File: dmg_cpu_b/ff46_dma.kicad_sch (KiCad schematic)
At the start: 71 parts

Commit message: First lot of fixes based on issues found.
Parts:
- removed LYXE: OR_2, symbol DMG_CPU_Cells:OR_2
- added LYXE: NOR_LATCH, symbol DMG_CPU_Cells:NOR_LATCH
- added PYSU: INVERTER_A, symbol DMG_CPU_Cells:INVERTER_A
- gave numbers to parts that had none: 1
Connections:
- net CPU_WR2: now also LAVY.1; no longer LAVY.2
- net FF46: now also LAVY.2; no longer LAVY.1
- net ~{DMA_PHI}: now also NAXY.2
- net at LENE.3 (D), LUVY.6 (Q): no longer NAXY.2
- net at LAPA.1, LOKO.3: now also LYXE.4 (RESET)
- net at MARU.1 (~{ENA}), MARU.3 (ENA), NAFA.1 (~{ENA})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: now also PYSU.2; no longer LORU.2
- net at LAVY.3, LORU.1, LUPA.1: now also LYXE.1 (SET)
- net at LUPA.2: now also LYXE.3 (Q)
- new net: LORU.2, PYSU.1
- no-connect marks 5 -> 6
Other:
- moved on the sheet: LAVY, LORU, LUPA, LUVY, MOLU, NYGO

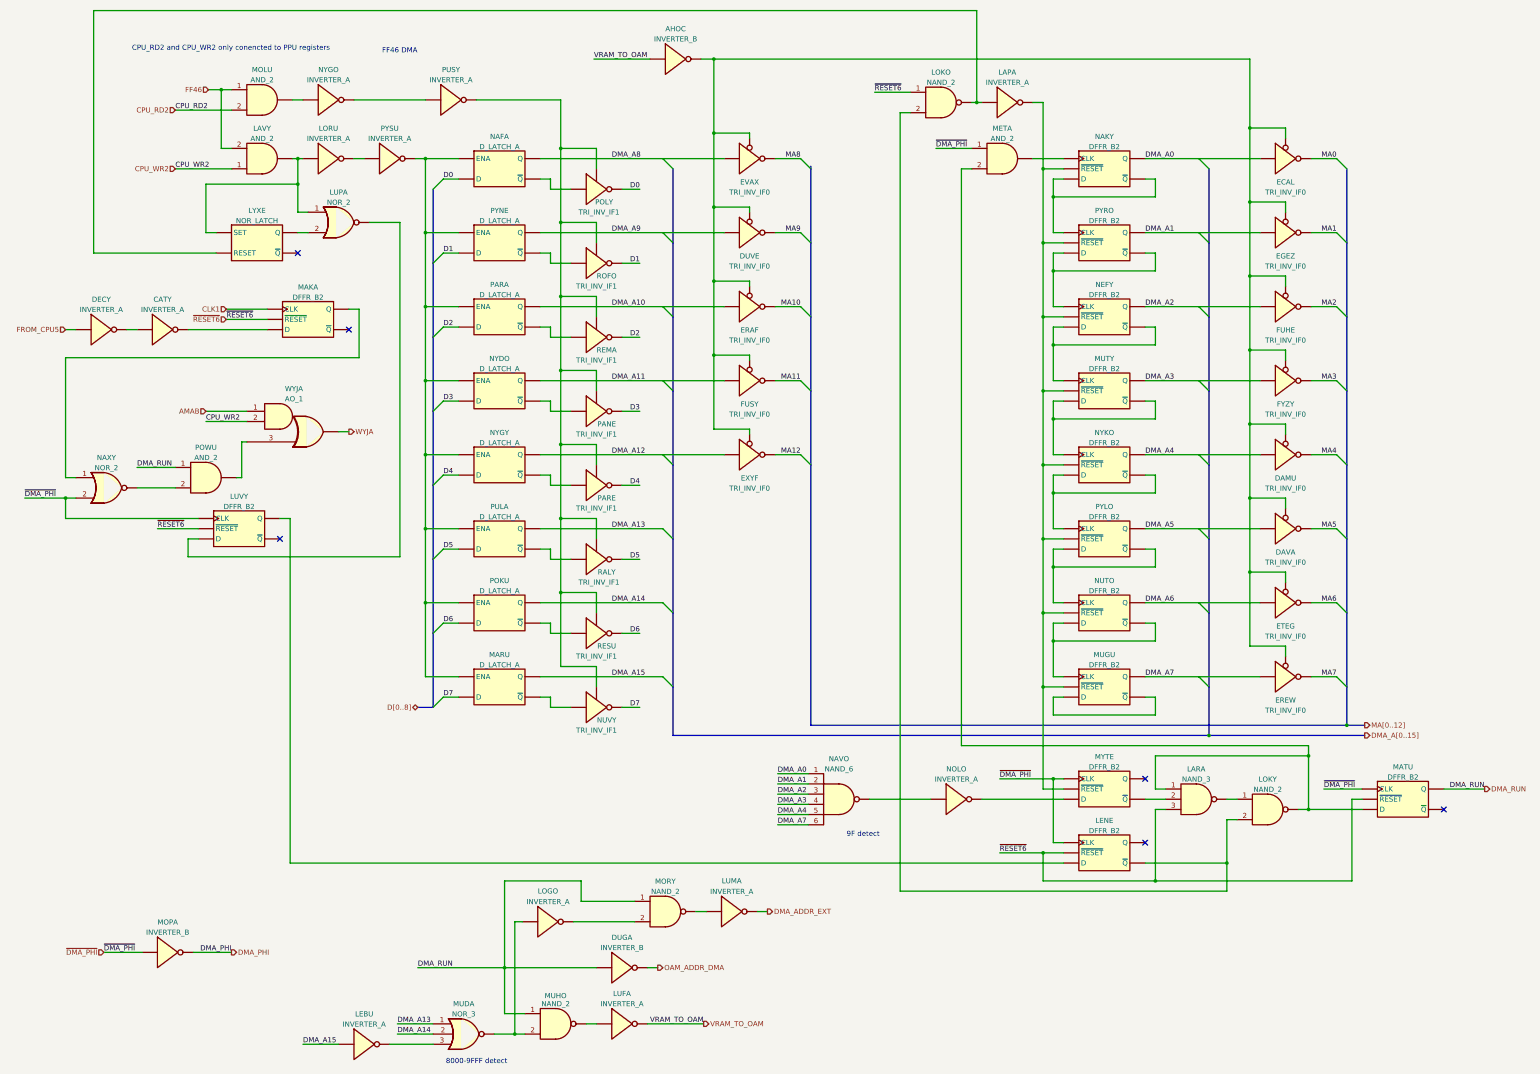
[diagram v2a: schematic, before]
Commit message: CH1 SWEEP page added.
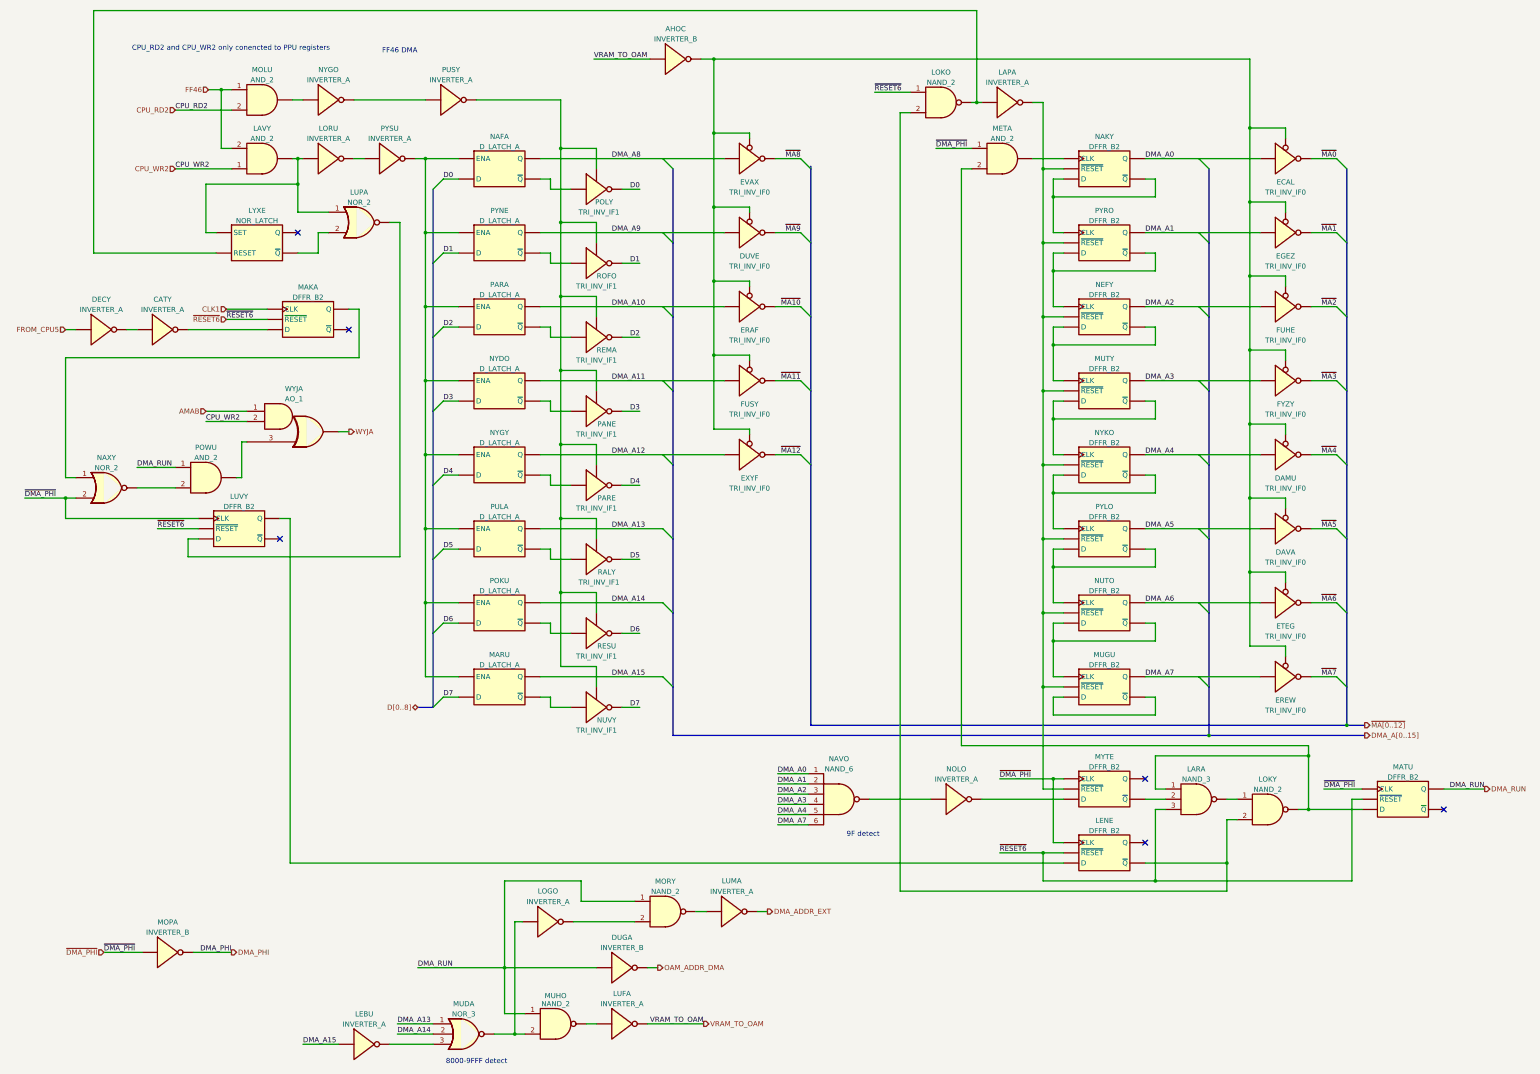
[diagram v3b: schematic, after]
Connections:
- net at LUPA.2: now also LYXE.2 (~{Q}); no longer LYXE.3 (Q)
- net MA0 renamed ~{MA0}
- net MA1 renamed ~{MA1}
- net MA10 renamed ~{MA10}
- net MA11 renamed ~{MA11}
- net MA12 renamed ~{MA12}
- net MA2 renamed ~{MA2}
- net MA3 renamed ~{MA3}
- net MA4 renamed ~{MA4}
- net MA5 renamed ~{MA5}
- net MA6 renamed ~{MA6}
- net MA7 renamed ~{MA7}
- net MA8 renamed ~{MA8}
- net MA9 renamed ~{MA9}
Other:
- moved on the sheet: LUPA
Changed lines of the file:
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@@
   )
   (no_connect (at 106.045 98.425))
-  (no_connect (at 93.345 79.375))
+  (no_connect (at 93.345 74.295))
   (no_connect (at 88.9 150.495))
   (no_connect (at 378.46 217.805))
@@
     (stroke (width 0) (type default) (color 0 0 0 0))
   )
-  (wire (pts (xy 118.745 71.755) (xy 111.125 71.755))
+  (wire (pts (xy 118.745 71.755) (xy 116.205 71.755))
     (stroke (width 0) (type default) (color 0 0 0 0))
   )
@@
     (stroke (width 0) (type default) (color 0 0 0 0))
   )
-  (wire (pts (xy 93.345 74.295) (xy 95.885 74.295))
-    (stroke (width 0) (type default) (color 0 0 0 0))
-  )
   (wire (pts (xy 42.545 19.05) (xy 42.545 79.375))
     (stroke (width 0) (type default) (color 0 0 0 0))
@@
     (stroke (width 0) (type default) (color 0 0 0 0))
   )
+  (wire (pts (xy 98.425 74.295) (xy 100.965 74.295))
+    (stroke (width 0) (type default) (color 0 0 0 0))
+  )
   (wire (pts (xy 144.78 257.175) (xy 144.78 235.585))
     (stroke (width 0) (type default) (color 0 0 0 0))
@@
     (stroke (width 0) (type default) (color 0 0 0 0))
   )
+  (wire (pts (xy 93.345 79.375) (xy 98.425 79.375))
+    (stroke (width 0) (type default) (color 0 0 0 0))
+  )
   (wire (pts (xy 283.845 113.665) (xy 278.765 113.665))
     (stroke (width 0) (type default) (color 0 0 0 0))
@@
     (stroke (width 0) (type default) (color 0 0 0 0))
   )
+  (wire (pts (xy 98.425 79.375) (xy 98.425 74.295))
+    (stroke (width 0) (type default) (color 0 0 0 0))
+  )
   (wire (pts (xy 156.21 171.45) (xy 156.21 173.99))
     (stroke (width 0) (type default) (color 0 0 0 0))
@@
     (stroke (width 0) (type default) (color 0 0 0 0))
   )
-  (wire (pts (xy 95.885 69.215) (xy 93.345 69.215))
+  (wire (pts (xy 100.965 69.215) (xy 93.345 69.215))
     (stroke (width 0) (type default) (color 0 0 0 0))
   )
@@
     (effects (font (size 1.27 1.27)) (justify left bottom))
   )
-  (label "MA5" (at 351.79 147.955 180)
-    (effects (font (size 1.27 1.27)) (justify right bottom))
-  )
-  (label "MA7" (at 351.79 184.785 180)
-    (effects (font (size 1.27 1.27)) (justify right bottom))
-  )
-  (label "MA6" (at 351.79 166.37 180)
+  (label "~{MA5}" (at 351.79 147.955 180)
+    (effects (font (size 1.27 1.27)) (justify right bottom))
+  )
+  (label "~{MA7}" (at 351.79 184.785 180)
+    (effects (font (size 1.27 1.27)) (justify right bottom))
+  )
+  (label "~{MA6}" (at 351.79 166.37 180)
     (effects (font (size 1.27 1.27)) (justify right bottom))
   )
@@
     (effects (font (size 1.27 1.27)) (justify left bottom))
   )
-  (label "MA8" (at 218.44 55.88 180)
+  (label "~{MA8}" (at 218.44 55.88 180)
     (effects (font (size 1.27 1.27)) (justify right bottom))
   )
@@
     (effects (font (size 1.27 1.27)) (justify left bottom))
   )
-  (label "MA2" (at 351.79 92.71 180)
-    (effects (font (size 1.27 1.27)) (justify right bottom))
-  )
-  (label "MA4" (at 351.79 129.54 180)
+  (label "~{MA2}" (at 351.79 92.71 180)
+    (effects (font (size 1.27 1.27)) (justify right bottom))
+  )
+  (label "~{MA4}" (at 351.79 129.54 180)
     (effects (font (size 1.27 1.27)) (justify right bottom))
   )
@@
     (effects (font (size 1.27 1.27)) (justify left bottom))
   )
-  (label "MA10" (at 218.44 92.71 180)
+  (label "~{MA10}" (at 218.44 92.71 180)
     (effects (font (size 1.27 1.27)) (justify right bottom))
   )
@@
     (effects (font (size 1.27 1.27)) (justify left bottom))
   )
-  (label "MA12" (at 218.44 129.54 180)
+  (label "~{MA12}" (at 218.44 129.54 180)
     (effects (font (size 1.27 1.27)) (justify right bottom))
   )
@@
     (effects (font (size 1.27 1.27)) (justify left bottom))
   )
-  (label "MA11" (at 218.44 111.125 180)
+  (label "~{MA11}" (at 218.44 111.125 180)
     (effects (font (size 1.27 1.27)) (justify right bottom))
   )
@@
     (effects (font (size 1.27 1.27)) (justify right bottom))
   )
-  (label "MA9" (at 218.44 74.295 180)
-    (effects (font (size 1.27 1.27)) (justify right bottom))
-  )
-  (label "MA0" (at 351.79 55.88 180)
+  (label "~{MA9}" (at 218.44 74.295 180)
+    (effects (font (size 1.27 1.27)) (justify right bottom))
+  )
+  (label "~{MA0}" (at 351.79 55.88 180)
     (effects (font (size 1.27 1.27)) (justify right bottom))
   )
@@
     (effects (font (size 1.27 1.27)) (justify left bottom))
   )
-  (label "MA3" (at 351.79 111.125 180)
+  (label "~{MA3}" (at 351.79 111.125 180)
     (effects (font (size 1.27 1.27)) (justify right bottom))
   )
@@
     (effects (font (size 1.27 1.27)) (justify left bottom))
   )
-  (label "MA1" (at 351.79 74.295 180)
+  (label "~{MA1}" (at 351.79 74.295 180)
     (effects (font (size 1.27 1.27)) (justify right bottom))
   )
@@
     (effects (font (size 1.27 1.27)) (justify right))
   )
-  (hierarchical_label "MA[0..12]" (shape output) (at 358.775 196.85 0)
+  (hierarchical_label "~{MA[0..12]}" (shape output) (at 358.775 196.85 0)
     (effects (font (size 1.27 1.27)) (justify left))
   )
@@
     (pin "1")
   )
-  (symbol (lib_id "DMG_CPU_Cells:NOR_2") (at 103.505 71.755 0) (unit 1)
+  (symbol (lib_id "DMG_CPU_Cells:NOR_2") (at 108.585 71.755 0) (unit 1)
     (in_bom yes) (on_board yes) (fields_autoplaced)
-    (property "Reference" "LUPA" (id 0) (at 103.5048 64.2452 0))
-    (property "Value" "NOR_2" (id 1) (at 103.5048 66.7821 0))
-    (property "Footprint" "" (id 2) (at 103.251 71.755 0)
-      (effects (font (size 1.27 1.27)) hide)
-    )
-    (property "Datasheet" "http://iceboy.a-singer.de/doc/dmg_cells.html#nor2" (id 3) (at 103.505 79.375 0)
-      (effects (font (size 1.27 1.27)) hide)
-    )
+    (property "Reference" "LUPA" (id 0) (at 108.5848 64.2452 0))
+    (property "Value" "NOR_2" (id 1) (at 108.5848 66.7821 0))
+    (property "Footprint" "" (id 2) (at 108.331 71.755 0)
+      (effects (font (size 1.27 1.27)) hide)
+    )
+    (property "Datasheet" "http://iceboy.a-singer.de/doc/dmg_cells.html#nor2" (id 3) (at 108.585 79.375 0)
+      (effects (font (size 1.27 1.27)) hide)
+    )

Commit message: BG and WIN sheets added.
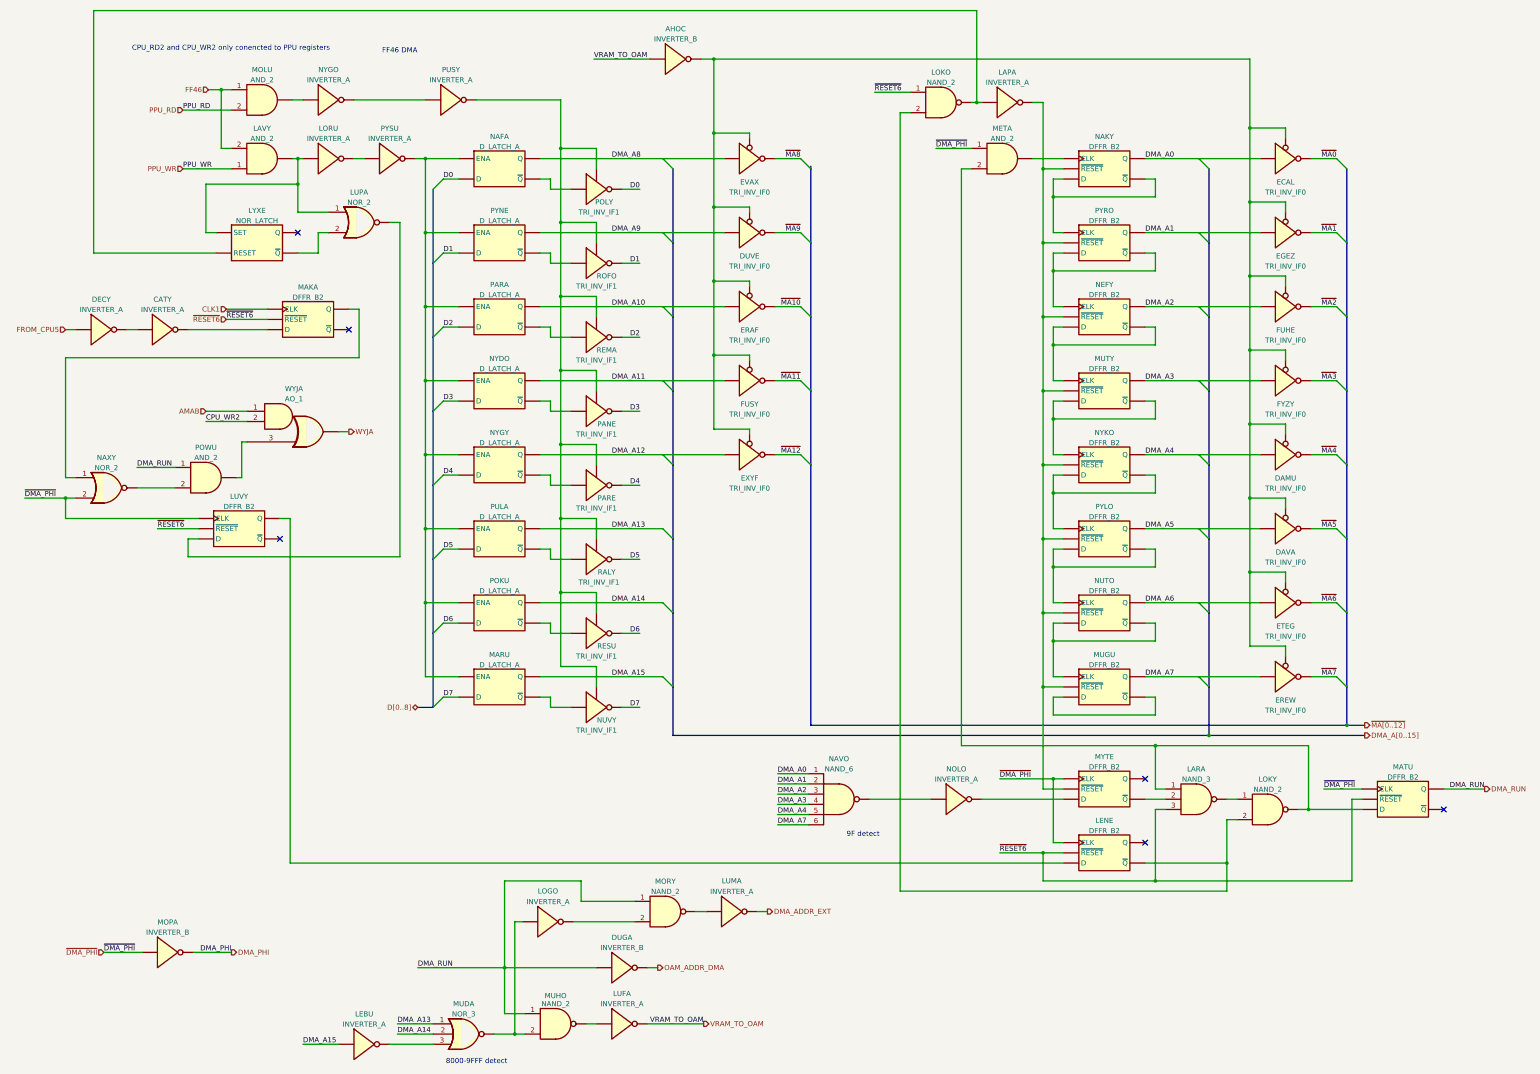
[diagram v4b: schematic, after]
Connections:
- net CPU_WR2: no longer LAVY.1
- net CPU_RD2 renamed PPU_RD
- new net PPU_WR: LAVY.1
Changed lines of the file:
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@@
   (junction (at 125.095 147.955) (diameter 0) (color 0 0 0 0)
   )
+  (junction (at 306.705 201.93) (diameter 0) (color 0 0 0 0)
+  )
   (junction (at 278.765 187.325) (diameter 0) (color 0 0 0 0)
   )
@@
   )
   (junction (at 330.2 103.505) (diameter 0) (color 0 0 0 0)
-  )
-  (junction (at 344.805 204.47) (diameter 0) (color 0 0 0 0)
   )
   (junction (at 330.2 48.26) (diameter 0) (color 0 0 0 0)
@@
     (stroke (width 0) (type default) (color 0 0 0 0))
   )
-  (wire (pts (xy 306.705 212.725) (xy 306.705 204.47))
+  (wire (pts (xy 306.705 212.725) (xy 306.705 201.93))
     (stroke (width 0) (type default) (color 0 0 0 0))
   )
@@
     (stroke (width 0) (type default) (color 0 0 0 0))
   )
-  (wire (pts (xy 62.865 43.815) (xy 76.835 43.815))
-    (stroke (width 0) (type default) (color 0 0 0 0))
-  )
   (wire (pts (xy 147.32 245.745) (xy 149.225 245.745))
     (stroke (width 0) (type default) (color 0 0 0 0))
@@
     (stroke (width 0) (type default) (color 0 0 0 0))
   )
-  (wire (pts (xy 258.445 201.93) (xy 344.805 201.93))
+  (wire (pts (xy 258.445 201.93) (xy 306.705 201.93))
     (stroke (width 0) (type default) (color 0 0 0 0))
   )
@@
     (stroke (width 0) (type default) (color 0 0 0 0))
   )
+  (wire (pts (xy 344.805 201.93) (xy 344.805 217.805))
+    (stroke (width 0) (type default) (color 0 0 0 0))
+  )
   (wire (pts (xy 267.97 228.6) (xy 278.765 228.6))
     (stroke (width 0) (type default) (color 0 0 0 0))
@@
     (stroke (width 0) (type default) (color 0 0 0 0))
   )
-  (wire (pts (xy 344.805 201.93) (xy 344.805 204.47))
-    (stroke (width 0) (type default) (color 0 0 0 0))
-  )
   (wire (pts (xy 125.095 147.955) (xy 133.35 147.955))
     (stroke (width 0) (type default) (color 0 0 0 0))
@@
     (stroke (width 0) (type default) (color 0 0 0 0))
   )
-  (wire (pts (xy 62.865 58.42) (xy 76.835 58.42))
-    (stroke (width 0) (type default) (color 0 0 0 0))
-  )
   (wire (pts (xy 283.845 134.62) (xy 281.305 134.62))
     (stroke (width 0) (type default) (color 0 0 0 0))
@@
     (stroke (width 0) (type default) (color 0 0 0 0))
   )
+  (wire (pts (xy 64.77 43.815) (xy 76.835 43.815))
+    (stroke (width 0) (type default) (color 0 0 0 0))
+  )
   (wire (pts (xy 137.795 41.275) (xy 158.75 41.275))
     (stroke (width 0) (type default) (color 0 0 0 0))
@@
     (stroke (width 0) (type default) (color 0 0 0 0))
   )
-  (wire (pts (xy 344.805 204.47) (xy 344.805 217.805))
-    (stroke (width 0) (type default) (color 0 0 0 0))
-  )
   (wire (pts (xy 75.565 93.345) (xy 85.725 93.345))
     (stroke (width 0) (type default) (color 0 0 0 0))
@@
     (stroke (width 0) (type default) (color 0 0 0 0))
   )
-  (wire (pts (xy 306.705 204.47) (xy 344.805 204.47))
+  (wire (pts (xy 306.705 201.93) (xy 344.805 201.93))
     (stroke (width 0) (type default) (color 0 0 0 0))
   )
@@
   )
   (wire (pts (xy 156.21 192.405) (xy 161.29 192.405))
+    (stroke (width 0) (type default) (color 0 0 0 0))
+  )
+  (wire (pts (xy 64.77 58.42) (xy 76.835 58.42))
     (stroke (width 0) (type default) (color 0 0 0 0))
   )
@@
     (effects (font (size 1.27 1.27)) (justify right bottom))
   )
-  (label "CPU_WR2" (at 62.865 58.42 0)
-    (effects (font (size 1.27 1.27)) (justify left bottom))
-  )
   (label "~{MA2}" (at 351.79 92.71 180)
     (effects (font (size 1.27 1.27)) (justify right bottom))
@@
     (effects (font (size 1.27 1.27)) (justify right bottom))
   )
+  (label "PPU_RD" (at 64.77 43.815 0)
+    (effects (font (size 1.27 1.27)) (justify left bottom))
+  )
   (label "D0" (at 178.435 63.5 180)
     (effects (font (size 1.27 1.27)) (justify right bottom))
@@
     (effects (font (size 1.27 1.27)) (justify right bottom))
   )
-  (label "CPU_RD2" (at 62.865 43.815 0)
-    (effects (font (size 1.27 1.27)) (justify left bottom))
-  )
   (label "DMA_A14" (at 171.45 166.37 0)
     (effects (font (size 1.27 1.27)) (justify left bottom))
@@
   (label "~{MA1}" (at 351.79 74.295 180)
     (effects (font (size 1.27 1.27)) (justify right bottom))
+  )
+  (label "PPU_WR" (at 64.77 58.42 0)
+    (effects (font (size 1.27 1.27)) (justify left bottom))
   )
   (label "~{RESET6}" (at 58.42 147.955 0)
@@
     (effects (font (size 1.27 1.27)) (justify right))
   )
-  (hierarchical_label "CPU_WR2" (shape input) (at 62.865 58.42 180)
-    (effects (font (size 1.27 1.27)) (justify right))
-  )
   (hierarchical_label "DMA_RUN" (shape output) (at 388.62 212.725 0)
     (effects (font (size 1.27 1.27)) (justify left))
@@
     (effects (font (size 1.27 1.27)) (justify right))
   )
-  (hierarchical_label "CPU_RD2" (shape input) (at 62.865 43.815 180)
-    (effects (font (size 1.27 1.27)) (justify right))
-  )
   (hierarchical_label "~{RESET6}" (shape input) (at 75.565 95.885 180)
     (effects (font (size 1.27 1.27)) (justify right))
@@
     (effects (font (size 1.27 1.27)) (justify left))
   )
+  (hierarchical_label "PPU_WR" (shape input) (at 64.77 58.42 180)
+    (effects (font (size 1.27 1.27)) (justify right))
+  )
+  (hierarchical_label "PPU_RD" (shape input) (at 64.77 43.815 180)
+    (effects (font (size 1.27 1.27)) (justify right))
+  )
   (hierarchical_label "DMA_PHI" (shape output) (at 76.835 253.365 0)
